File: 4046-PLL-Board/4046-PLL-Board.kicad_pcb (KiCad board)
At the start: 2 copper layers, 50 x 40 mm, 53 parts, among them J1 Conn_01x02_Pin, J2 Conn_02x03_Odd_Even, J3 Conn_01x02_Pin, J4 Conn_01x02_Pin, J5 Conn_01x02_Pin, J6 Conn_01x03_Pin, U1 CD4046, U2 74LVC2G04, U3 L78M05

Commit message: add MOSFET Driver design files and author info
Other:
- board text added: "De.by Jas.C 2025.10.28"
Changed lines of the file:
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@@
 	(title_block
 		(title "4046 PLL Board")
-		(date "2025-10-27")
+		(date "2025-10-28")
 		(rev "1.0.0")
 		(company "Jason Chen")
@@
 		)
 	)
+	(gr_text "De.by Jas.C\n2025.10.28"
+		(at 144.3 108.1 0)
+		(layer "B.SilkS" knockout)
+		(effects
+			(font
+				(size 1 1)
+				(thickness 0.15)
+			)
+			(justify bottom mirror)
+		)
+	)

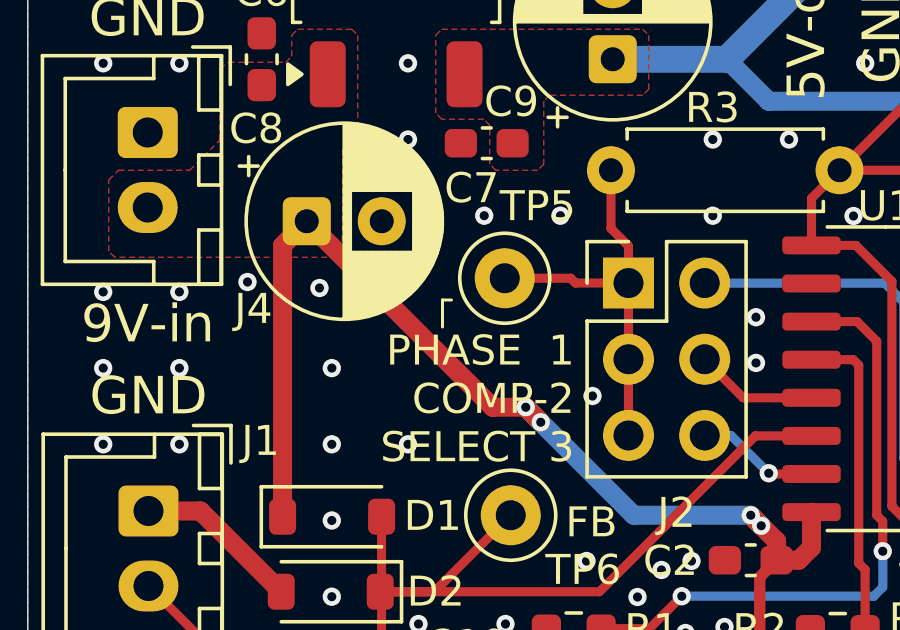
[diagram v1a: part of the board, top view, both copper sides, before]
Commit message: add IXD614 GDT Driver design REV 1.0.0
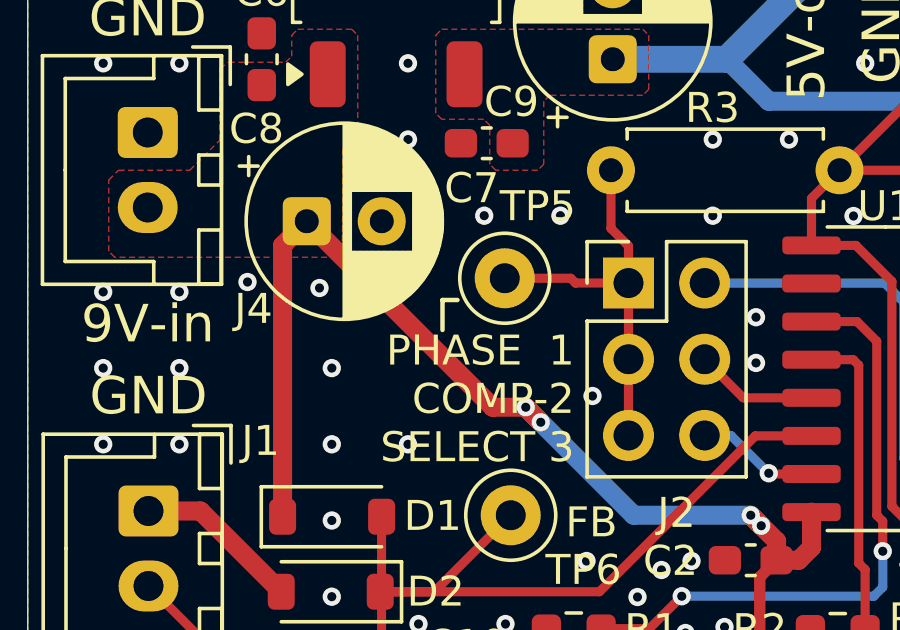
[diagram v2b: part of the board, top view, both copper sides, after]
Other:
- board text added: "Designed by Jason Chen. 2025.10.28"
- board text removed: "De.by Jas.C 2025.10.28"

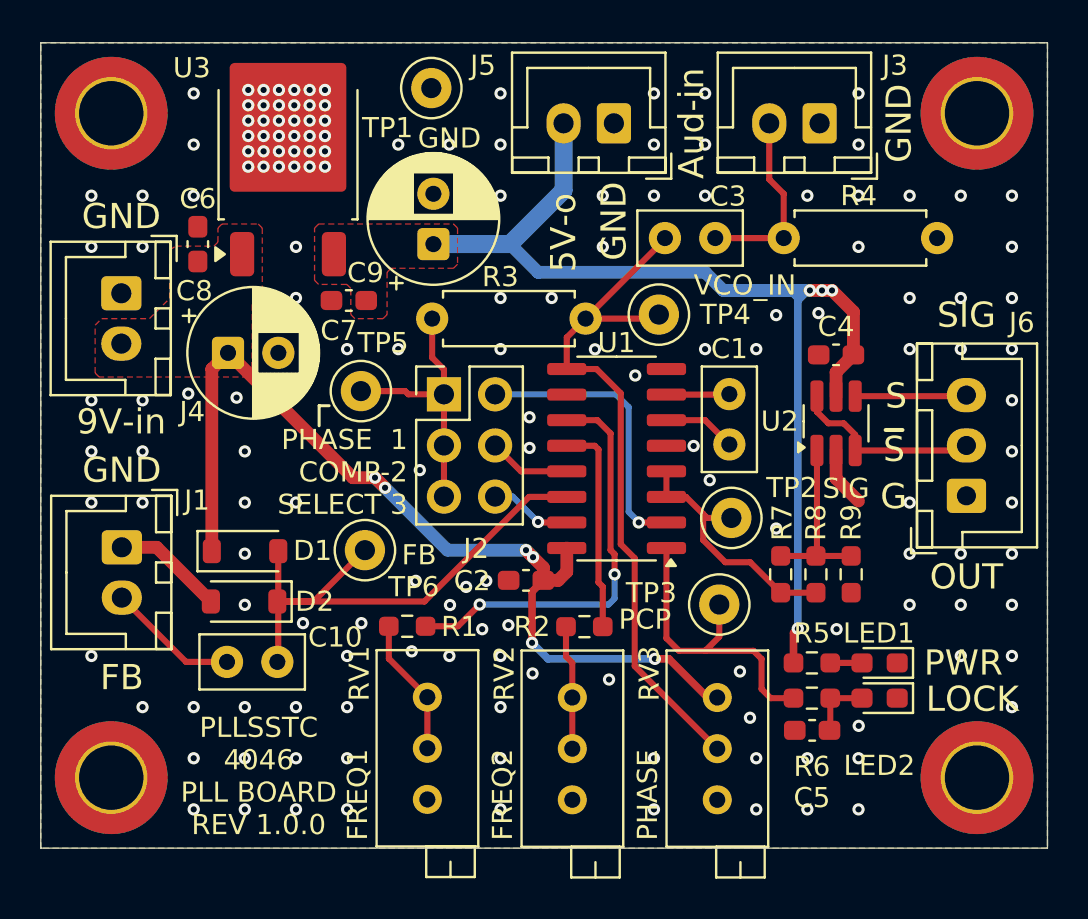
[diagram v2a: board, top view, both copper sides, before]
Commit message: add support for CD4046 in SO-16-208mil package on PLL board
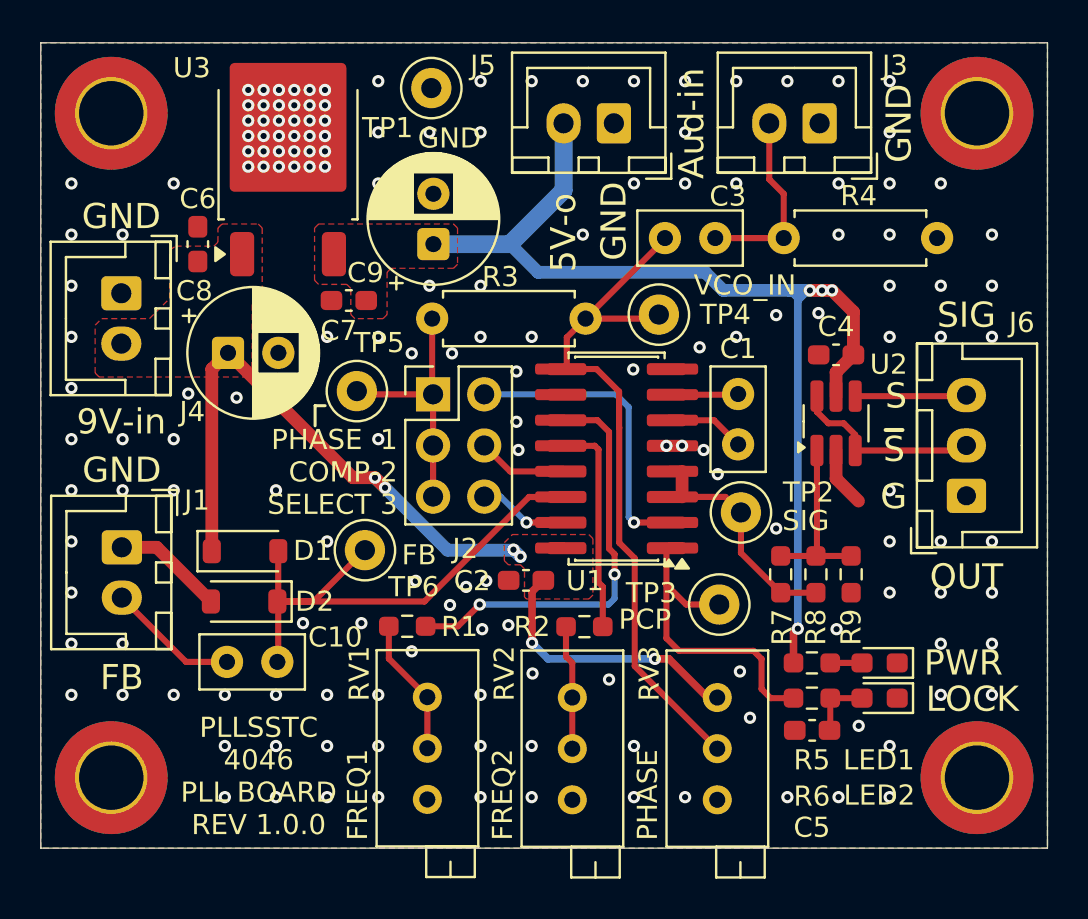
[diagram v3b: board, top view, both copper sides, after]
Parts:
- added U4: CD4046, Package_SO:SOIC-16_3.9x9.9mm_P1.27mm, F.Cu at (150.4, 98.8)
- U1: footprint Package_SO:SOIC-16_3.9x9.9mm_P1.27mm -> Package_SO:SOIC-16_4.55x10.3mm_P1.27mm
- moved TP2 0.55 mm to (156.6, 101.5)
- moved J2 0.54 mm to (141.3, 95.6)
- moved C1 0.44 mm to (156.4, 98.1)
- moved TP5 0.20 mm to (137.5, 95.5)
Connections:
- net Net-(U1-C1) renamed /CD4046_C1
- net Net-(U1-C2) renamed /CD4046_C2
- net Net-(U1-R1) renamed /CD4046_R1
- net Net-(U1-R2) renamed /CD4046_R2
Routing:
- net +9V: track 48.4 -> 43.3 mm
- net /SIG: track 12.9 -> 11.1 mm
- net /PHASE_COMP_1: track 14.2 -> 15.7 mm
- net /VCO_IN: track 35.1 -> 35.8 mm
- net /CD4046_R2: track 10.5 -> 11.3 mm
- net /CD4046_R1: track 20.7 -> 21.5 mm
- net /PHASE_COMP: track 13.3 -> 12.7 mm
- net /PHASE_COMP_2: track 4.09 -> 4.63 mm
- net /PHASE_COMP_3: track 4.09 -> 4.63 mm
- net GND: vias 160 -> 165

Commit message: modified stitching vias
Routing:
- net GND: vias 165 -> 174
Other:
- board text added: "(⌐■_■)"
